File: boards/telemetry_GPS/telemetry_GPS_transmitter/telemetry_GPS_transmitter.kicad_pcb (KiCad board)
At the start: 4 copper layers, 98 x 57.1 mm, 67 parts, among them J1 Conn_02x05_Odd_Even, J2 Conn_01x03, J3 Conn_01x03, J4 Conn_Coaxial, J5 54602-908LF, SW1 SW_Push, U1 STM32WL55CCUx, U2 TLV75509PDBV, U4 BALFHB-WL-02D3, U5 MASW-007221, U6 NEO-M8N, U7 ISO1042QDWVQ1, U8 MCP2515-xST

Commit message: Pushing latest fixes
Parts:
- C1, C10, C11, C12, C13, C14, C15, C16, C17, C18, C19, C2, C20, C22, C23, C24, C3, C4, C5, C6, C7, C8, C9: footprint Capacitor_SMD:C_0603_1608Metric_Pad1.08x0.95mm_HandSolder -> Capacitor_SMD:C_0603_1608Metric
- R1, R10, R11, R12, R13, R14, R15, R2, R3, R4, R5, R6, R7, R8, R9: footprint Resistor_SMD:R_0603_1608Metric_Pad0.98x0.95mm_HandSolder -> Resistor_SMD:R_0603_1608Metric
- moved U8 0.14 mm to (147.5, 88.6)
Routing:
- net GND: track 117.1 -> 69.7 mm, vias 84 -> 144
- net +3V3: track 87.7 -> 84.4 mm
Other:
- rule pad_to_mask_clearance: 0 -> 0.075

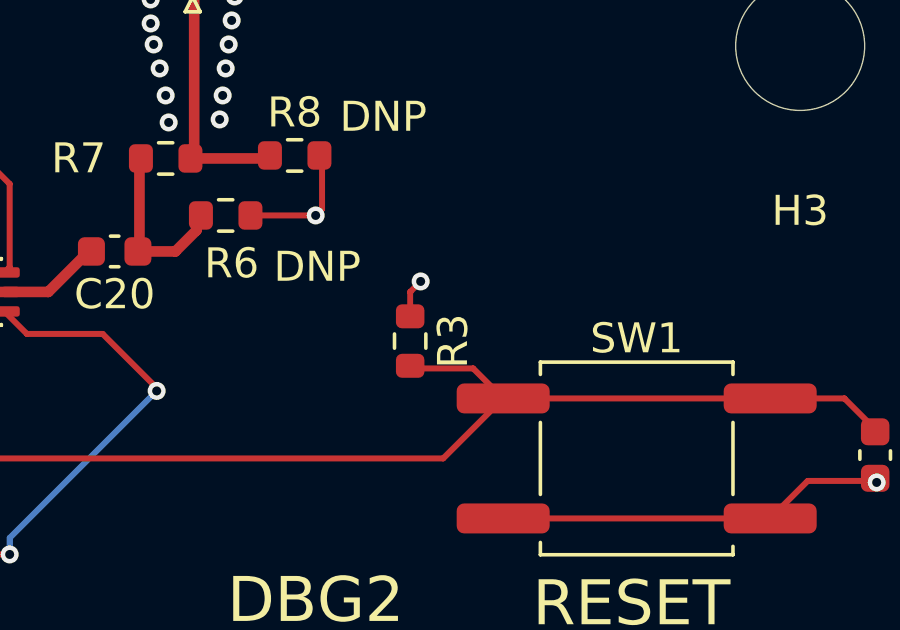
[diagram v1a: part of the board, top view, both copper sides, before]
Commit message: Made a resistor bigger so I can order from ECE Shop
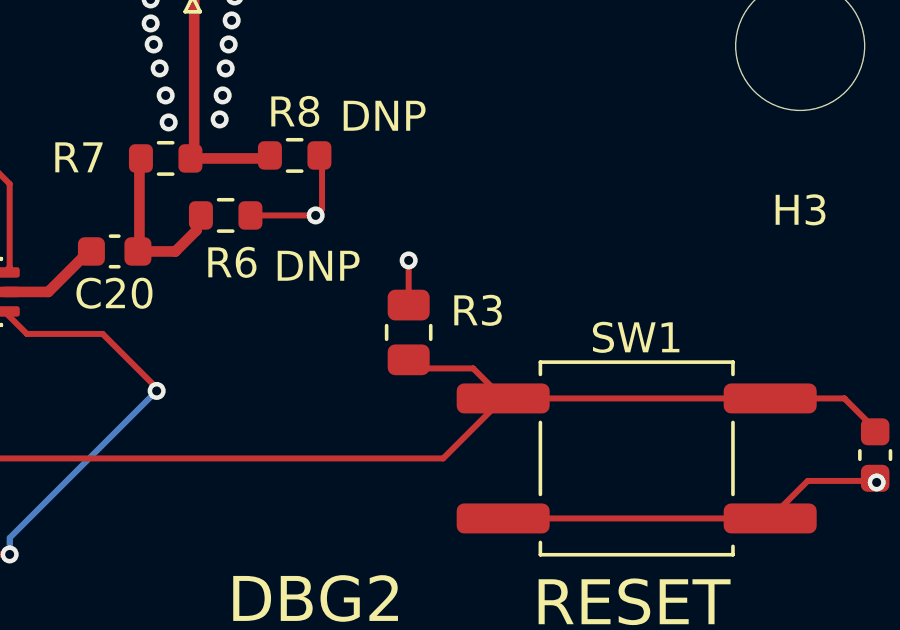
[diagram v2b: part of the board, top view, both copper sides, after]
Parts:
- C9: value 10nF -> 0.01uF
- R3: footprint Resistor_SMD:R_0603_1608Metric -> Resistor_SMD:R_0805_2012Metric
- moved R3 0.29 mm to (190.7, 76.8)
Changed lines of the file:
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@@
 		)
 	)
-	(footprint "Resistor_SMD:R_0603_1608Metric"
+	(footprint "Resistor_SMD:R_0805_2012Metric"
 		(layer "F.Cu")
-		(at 190.75 77.0875 -90)
-		(descr "Resistor SMD 0603 (1608 Metric), square (rectangular) end terminal, IPC-7351 nominal, (Body size source: IPC-SM-782 page 72, https://www.pcb-3d.com/wordpress/wp-content/uploads/ipc-sm-782a_amendment_1_and_2.pdf)")
+		(at 190.7 76.8 -90)
+		(descr "Resistor SMD 0805 (2012 Metric), square (rectangular) end terminal, IPC-7351 nominal, (Body size source: IPC-SM-782 page 72, https://www.pcb-3d.com/wordpress/wp-content/uploads/ipc-sm-782a_amendment_1_and_2.pdf)")
 		(tags "resistor")
 		(property "Reference" "R3"
-			(at 0 -1.43 270)
+			(at -0.7 -2.3 0)
 			(layer "F.SilkS")
 			(effects
@@
 		)
 		(property "Value" "100k"
-			(at 0 1.43 270)
+			(at 0 1.65 270)
 			(layer "F.Fab")
 			(effects
@@
 		(duplicate_pad_numbers_are_jumpers no)
 		(fp_line
-			(start -0.237258 0.5225)
-			(end 0.237258 0.5225)
+			(start -0.227064 0.735)
+			(end 0.227064 0.735)
 			(stroke
 				(width 0.12)
@@
 		)
 		(fp_line
-			(start -0.237258 -0.5225)
-			(end 0.237258 -0.5225)
+			(start -0.227064 -0.735)
+			(end 0.227064 -0.735)
 			(stroke
 				(width 0.12)
@@
 		)
 		(fp_rect
-			(start -1.48 -0.73)
-			(end 1.48 0.73)
+			(start -1.68 -0.95)
+			(end 1.68 0.95)
 			(stroke
 				(width 0.05)
@@
 		)
 		(fp_rect
-			(start -0.8 -0.4125)
-			(end 0.8 0.4125)
+			(start -1 -0.625)
+			(end 1 0.625)
 			(stroke
 				(width 0.1)
@@
 			(effects
 				(font
-					(size 0.4 0.4)
-					(thickness 0.06)
+					(size 0.5 0.5)
+					(thickness 0.08)
 				)
 			)
 		)
 		(pad "1" smd roundrect
-			(at -0.825 0 270)
-			(size 0.8 0.95)
+			(at -0.9125 0 270)
+			(size 1.025 1.4)
 			(layers "F.Cu" "F.Mask" "F.Paste")
-			(roundrect_rratio 0.25)
+			(roundrect_rratio 0.243902)
 			(net "+3V3")
 			(pintype "passive")
 		)
 		(pad "2" smd roundrect
-			(at 0.825 0 270)
-			(size 0.8 0.95)
+			(at 0.9125 0 270)
+			(size 1.025 1.4)
 			(layers "F.Cu" "F.Mask" "F.Paste")
-			(roundrect_rratio 0.25)
+			(roundrect_rratio 0.243902)
 			(net "/Debug/NRST")
 			(pintype "passive")
 		)
 		(embedded_fonts no)
-		(model "${KICAD10_3DMODEL_DIR}/Resistor_SMD.3dshapes/R_0603_1608Metric.step"
+		(model "${KICAD10_3DMODEL_DIR}/Resistor_SMD.3dshapes/R_0805_2012Metric.step"
 			(offset
 				(xyz 0 0 0)
@@
 			)
 		)
-		(property "Value" "10nF"
+		(property "Value" "0.01uF"
 			(at 0 -1.43 0)
 			(layer "B.Fab")
@@
 	)
 	(segment
-		(start 190.75 75.45)
-		(end 191.1 75.1)
-		(width 0.2)
-		(layer "F.Cu")
-		(net "+3V3")
-	)
-	(segment
 		(start 144.455 96.605)
 		(end 145.2 97.35)
@@
 	)
 	(segment
+		(start 190.7 75.8875)
+		(end 190.7 74.4)
+		(width 0.2)
+		(layer "F.Cu")
+		(net "+3V3")
+	)
+	(segment
 		(start 141.988022 96.605)
 		(end 144.455 96.605)
@@
 	)
 	(segment
-		(start 190.75 76.175)
-		(end 190.75 75.45)
-		(width 0.2)
-		(layer "F.Cu")
-		(net "+3V3")
-	)
-	(segment
 		(start 156 77.6)
 		(end 155.75 77.35)
@@
 	)
 	(via blind
+		(at 190.7 74.4)
+		(size 0.6)
+		(drill 0.3)
+		(layers "F.Cu" "In2.Cu")
+		(net "+3V3")
+	)
+	(via blind
 		(at 154.3 74.7)
 		(size 0.6)
@@
 		(net "+3V3")
 	)
-	(via blind
-		(at 191.1 75.1)
-		(size 0.6)
-		(drill 0.3)
-		(layers "F.Cu" "In2.Cu")
-		(net "+3V3")
-	)
 	(via
 		(at 155.5 74.15)
@@
 	)
 	(segment
-		(start 192.85 78)
-		(end 193.85 79)
+		(start 205.225 79)
+		(end 206.25 80.025)
 		(width 0.2)
 		(layer "F.Cu")
@@
 	)
 	(segment
-		(start 205.225 79)
-		(end 206.25 80.025)
+		(start 166.284314 77.1)
+		(end 170.184314 81)
 		(width 0.2)
 		(layer "F.Cu")
@@
 	)
 	(segment
-		(start 190.75 78)
-		(end 192.85 78)
+		(start 192.85 78)
+		(end 193.85 79)
 		(width 0.2)
 		(layer "F.Cu")
@@
 	)
 	(segment
-		(start 166.284314 77.1)
-		(end 170.184314 81)
+		(start 190.7 77.7125)
+		(end 190.9875 78)
+		(width 0.2)
+		(layer "F.Cu")
+		(net "/Debug/NRST")
+	)
+	(segment
+		(start 190.9875 78)
+		(end 192.85 78)
 		(width 0.2)
 		(layer "F.Cu")

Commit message: Pushing finalized design
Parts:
- D4: footprint Diode_SMD:D_0603_1608Metric_Pad1.05x0.95mm_HandSolder -> 1N4148WS:SODFL2512X90N
- L1: footprint Inductor_SMD:L_0603_1608Metric_Pad1.05x0.95mm_HandSolder -> Inductor_SMD:L_0805_2012Metric
- moved J2 35.2 mm to (122.5, 86.4), turned to 0 degrees
- moved D1 6.05 mm to (119.0, 96.1)
- moved R2 5.03 mm to (119.0, 99.7)
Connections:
- J2 pad 1: /Debug/MCU_UART_RX -> /Debug/MCU_UART_TX
- J2 pad 2: /Debug/MCU_UART_TX -> /Debug/MCU_UART_RX
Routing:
- net /Debug/MCU_UART_RX: track 24.3 -> 44.0 mm
- net /Debug/MCU_UART_TX: track 24.8 -> 41.9 mm
- net Net-(D1-K): track 2.70 -> 1.76 mm

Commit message: added more vias
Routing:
- net GND: vias 144 -> 152
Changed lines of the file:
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@@
+	)
+	(via blind
+		(at 183.4 98.7)
+		(size 0.6)
+		(drill 0.3)
+		(layers "F.Cu" "In1.Cu")
+		(free yes)
+		(net "GND")
 	)
 	(via blind
@@
 	)
 	(via blind
+		(at 182.918765 99.297435)
+		(size 0.6)
+		(drill 0.3)
+		(layers "F.Cu" "In1.Cu")
+		(free yes)
+		(net "GND")
+	)
+	(via blind
 		(at 172.8 71.2)
 		(size 0.6)
@@
 	)
 	(via blind
+		(at 181.931107 99.283122)
+		(size 0.6)
+		(drill 0.3)
+		(layers "F.Cu" "In1.Cu")
+		(free yes)
+		(net "GND")
+	)
+	(via blind
 		(at 129.2 78.2)
 		(size 0.6)
@@
 	)
 	(via blind
+		(at 181.3 100.8)
+		(size 0.6)
+		(drill 0.3)
+		(layers "F.Cu" "In1.Cu")
+		(free yes)
+		(net "GND")
+	)
+	(via blind
 		(at 206.4 104.9)
 		(size 0.6)
@@
 	)
 	(via blind
+		(at 181.4 98.7)
+		(size 0.6)
+		(drill 0.3)
+		(layers "F.Cu" "In1.Cu")
+		(free yes)
+		(net "GND")
+	)
+	(via blind
 		(at 186.9 100.6)
 		(size 0.6)
@@
 	)
 	(via blind
+		(at 183.906424 99.354691)
+		(size 0.6)
+		(drill 0.3)
+		(layers "F.Cu" "In1.Cu")
+		(free yes)
+		(net "GND")
+	)
+	(via blind
 		(at 163.1 98.9)
 		(size 0.6)
@@
 	)
 	(via blind
+		(at 180.9 99.3)
+		(size 0.6)
+		(drill 0.3)
+		(layers "F.Cu" "In1.Cu")
+		(free yes)
+		(net "GND")
+	)
+	(via blind
 		(at 159.700612 75.496601)
 		(size 0.6)
@@
 		(size 0.6)
 		(drill 0.3)
+		(layers "F.Cu" "In1.Cu")
+		(free yes)
+		(net "GND")
+	)
+	(via blind
+		(at 183.3 100.8)
+		(size 0.6)
+		(drill 0.3)

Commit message: I forgot to save so I'm pushing again
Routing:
- net GND: vias 152 -> 148
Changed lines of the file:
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@@
-	)
-	(via blind
-		(at 182.918765 99.297435)
-		(size 0.6)
-		(drill 0.3)
-		(layers "F.Cu" "In1.Cu")
-		(free yes)
-		(net "GND")
 	)
 	(via blind
@@
 	)
 	(via blind
-		(at 181.931107 99.283122)
-		(size 0.6)
-		(drill 0.3)
-		(layers "F.Cu" "In1.Cu")
-		(free yes)
-		(net "GND")
-	)
-	(via blind
 		(at 129.2 78.2)
 		(size 0.6)
@@
 	)
 	(via blind
-		(at 183.906424 99.354691)
-		(size 0.6)
-		(drill 0.3)
-		(layers "F.Cu" "In1.Cu")
-		(free yes)
-		(net "GND")
-	)
-	(via blind
 		(at 163.1 98.9)
 		(size 0.6)
@@
 		(size 0.6)
 		(drill 0.3)
-		(layers "F.Cu" "In1.Cu")
-		(free yes)
-		(net "GND")
-	)
-	(via blind
-		(at 180.9 99.3)
-		(size 0.6)
-		(drill 0.3)

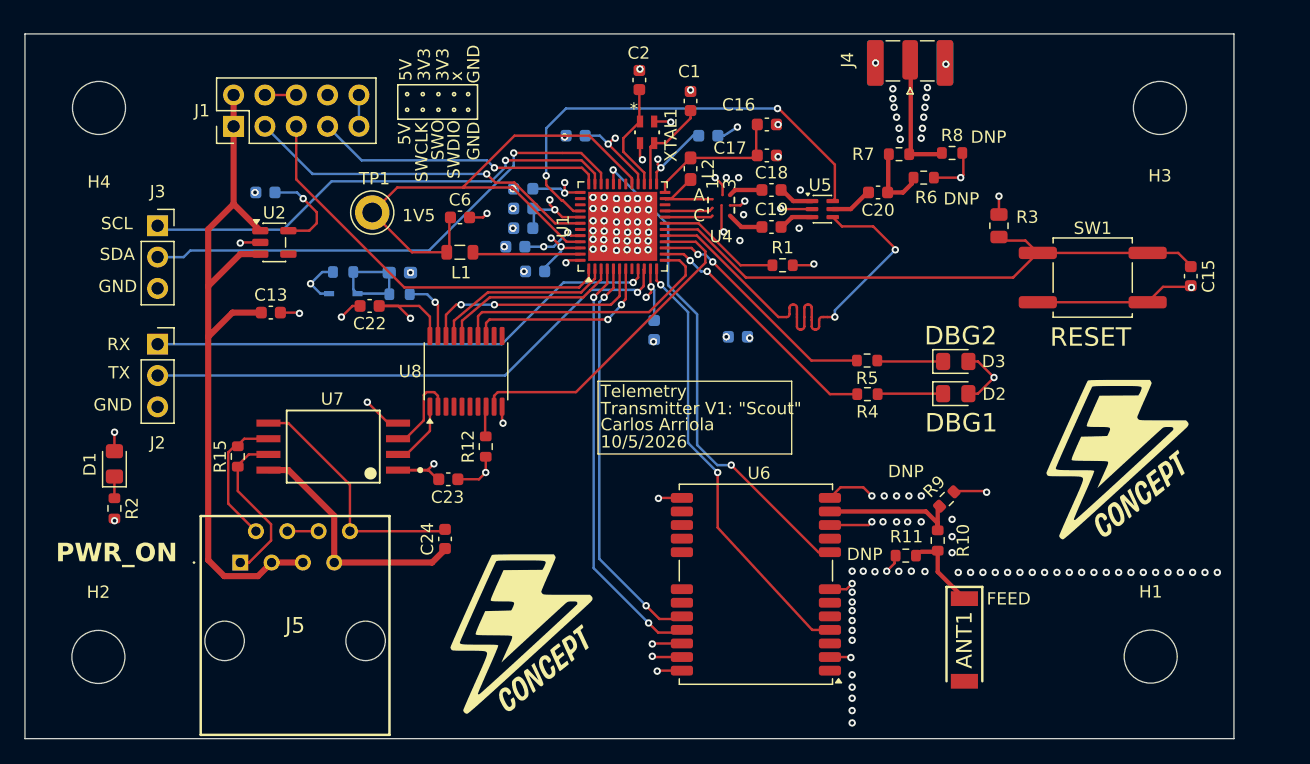
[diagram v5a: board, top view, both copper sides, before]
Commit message: Swapped out blind vias for through vias, added rounded edges, decreased L2 footprint
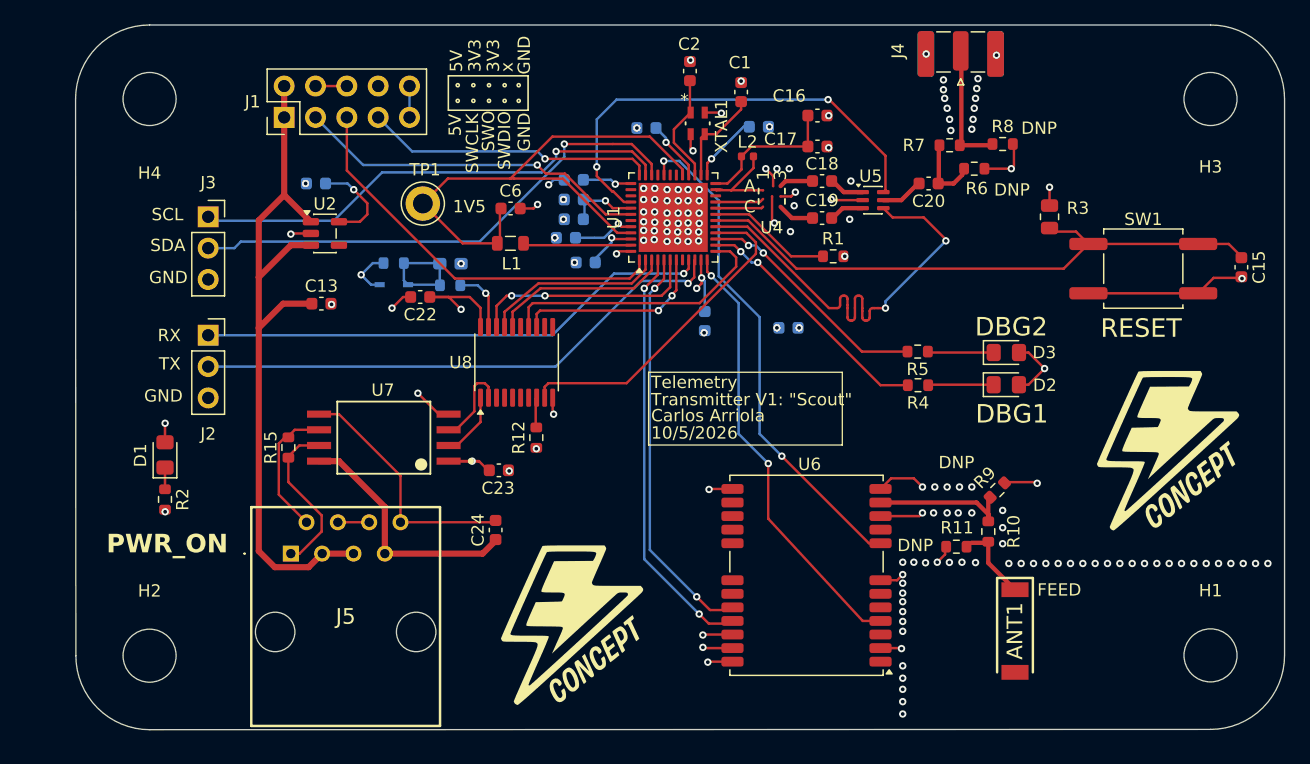
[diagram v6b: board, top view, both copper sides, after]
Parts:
- L2: footprint Inductor_SMD:L_0603_1608Metric_Pad1.05x0.95mm_HandSolder -> Inductor_SMD:L_0402_1005Metric
- moved C5 5.77 mm to (162.1, 68.9)
- moved H1 4.85 mm to (207.8, 111.6)
- moved L2 4.72 mm to (170.3, 71.2), turned to 0 degrees
- moved C16 4.16 mm to (176.0, 67.9)
- moved C18 4.16 mm to (176.4, 73.2)
- moved C19 4.16 mm to (176.4, 76.2)
- moved C9 4.16 mm to (156.2, 74.7)
- moved U5 4.16 mm to (180.5, 74.7)
- moved C1 4.16 mm to (169.8, 66.0)
- moved C11 4.16 mm to (156.2, 76.3)
- moved C12 4.16 mm to (156.2, 73.1)
- moved C17 4.16 mm to (176.0, 70.4)
- moved C21 4.16 mm to (146.2, 79.9)
- moved C3 4.16 mm to (171.2, 68.8)
- moved C6 4.16 mm to (151.1, 75.4)
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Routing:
- net GND: track 69.7 -> 62.7 mm, vias 148 -> 147
- net +3V3: track 84.7 -> 78.1 mm, vias 25 -> 19
- net /RF/RFO_HP: track 6.56 -> 7.86 mm
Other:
- outline, holes or cut-outs redrawn

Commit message: Okay now it's finally fixed
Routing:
- net GND: track 62.7 -> 93.5 mm
- net +3V3: track 78.1 -> 76.5 mm
